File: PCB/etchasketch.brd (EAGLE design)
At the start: 164 x 115 mm, 11 parts

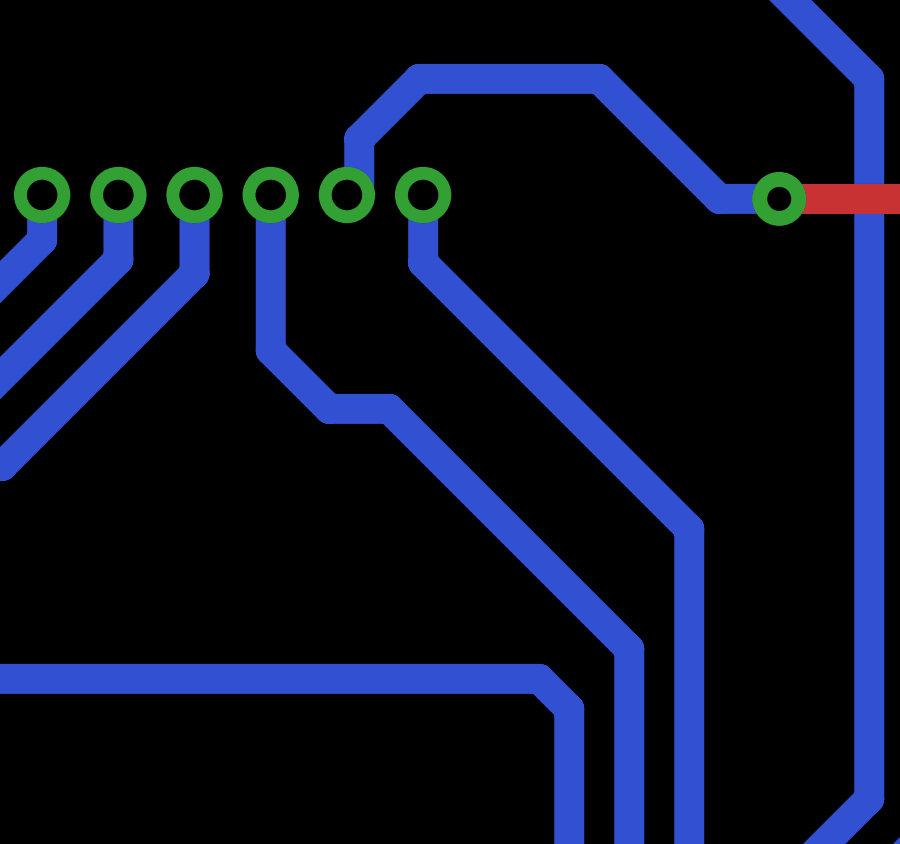
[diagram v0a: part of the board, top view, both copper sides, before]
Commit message: Modifiy traces
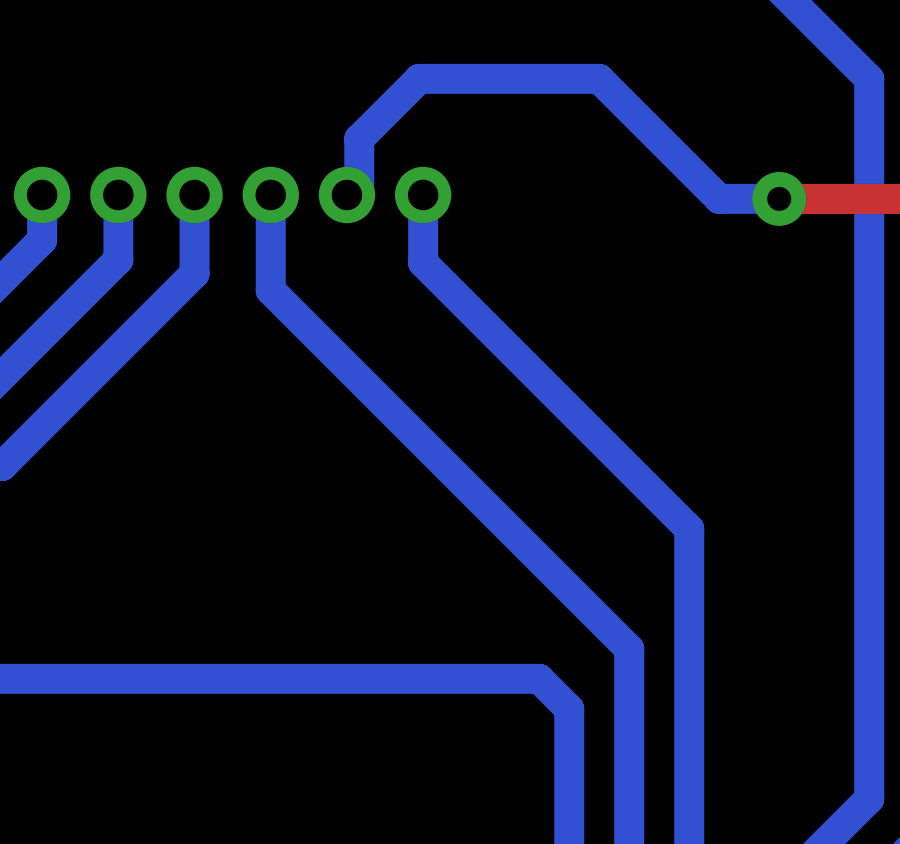
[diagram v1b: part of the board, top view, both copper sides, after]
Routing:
- net N$2: track 122.4 -> 121.2 mm
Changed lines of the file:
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@@
 <wire x1="95" y1="38.81" x2="95" y2="12" width="1" layer="16"/>
 <wire x1="79.5" y1="6.5" x2="74" y2="12" width="1" layer="16"/>
-<wire x1="66" y1="50" x2="64" y2="50" width="1" layer="16"/>
-<wire x1="64" y1="50" x2="62.05" y2="51.95" width="1" layer="16"/>
-<wire x1="62.05" y1="51.95" x2="62.05" y2="57.13" width="1" layer="16"/>
+<wire x1="62.05" y1="53.95" x2="62.05" y2="57.13" width="1" layer="16"/>
 <wire x1="74" y1="12" x2="74" y2="42" width="1" layer="16"/>
-<wire x1="74" y1="42" x2="66" y2="50" width="1" layer="16"/>
+<wire x1="74" y1="42" x2="62.05" y2="53.95" width="1" layer="16"/>
 <wire x1="103.75" y1="43.5" x2="103.5" y2="43.5" width="1" layer="16"/>
 <wire x1="103.5" y1="43.5" x2="101.595" y2="45.405" width="1" layer="16"/>

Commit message: update
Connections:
- net N$2 renamed PUSHBUTTON
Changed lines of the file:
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@@
 <wire x1="76" y1="46" x2="67.13" y2="54.87" width="1" layer="16"/>
 </signal>
-<signal name="N$2">
+<signal name="PUSHBUTTON">
 <contactref element="S1" pad="1"/>
 <contactref element="B1" pad="A3"/>
